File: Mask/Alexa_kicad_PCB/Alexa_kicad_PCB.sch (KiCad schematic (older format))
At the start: 28 parts

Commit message: changed op amp to tlv2372
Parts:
- removed U?: OPAMP, symbol pspice:OPAMP
- added U? (x2): TLV2372, symbol Amplifier_Operational:TLV2372
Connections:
- net labels added: EYES_SERVO, MOUTH_SERVO, NECK_SERVO
- wire segments 86 -> 100
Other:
- moved on the sheet: C?, M?, R?

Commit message: changed 3.5mm jack to 1503 09 part symbol
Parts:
- removed J?: Audio In, symbol Connector:AudioJack2_Ground
- removed J?: Audio Out, symbol Connector:AudioJack2_Ground
- added X? (x2): 1503_09, 1503_09, symbol Kicad_symbols:1503_09
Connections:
- wire segments 100 -> 104
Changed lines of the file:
@@
 	6200 4150 6200 4200
-$Comp
-L Connector:AudioJack2_Ground J?
-U 1 1 5F09035A
-P 1050 6350
-F 0 "J?" H 1082 6675 50  0000 C CNN
-F 1 "Audio In" H 1082 6584 50  0000 C CNN
-F 2 "" H 1050 6350 50  0001 C CNN
-F 3 "~" H 1050 6350 50  0001 C CNN
-	1    1050 6350
-	1    0    0    -1
-$EndComp
-$Comp
-L Connector:AudioJack2_Ground J?
-U 1 1 5F094637
-P 1050 7050
-F 0 "J?" H 1082 7375 50  0000 C CNN
-F 1 "Audio Out" H 1082 7284 50  0000 C CNN
-F 2 "" H 1050 7050 50  0001 C CNN
-F 3 "~" H 1050 7050 50  0001 C CNN
-	1    1050 7050
-	1    0    0    -1
-$EndComp
-Wire Wire Line
-	1250 6250 1400 6250
-Wire Wire Line
-	1400 6250 1400 6450
-Wire Wire Line
-	1400 6950 1250 6950
-Wire Wire Line
-	1250 6350 1450 6350
-Wire Wire Line
-	1450 6350 1450 6450
-Wire Wire Line
-	1450 7050 1250 7050
 $Comp
 L Device:R_Small R?
@@
 ADC_0
 $Comp
-L power:GND #PWR?
-U 1 1 5F1297DD
-P 1050 6500
-F 0 "#PWR?" H 1050 6250 50  0001 C CNN
-F 1 "GND" H 1150 6400 50  0000 C CNN
-F 2 "" H 1050 6500 50  0001 C CNN
-F 3 "" H 1050 6500 50  0001 C CNN
-	1    1050 6500
-	1    0    0    -1
-$EndComp
-$Comp
-L power:GND #PWR?
-U 1 1 5F12A17D
-P 1050 7250
-F 0 "#PWR?" H 1050 7000 50  0001 C CNN
-F 1 "GND" H 1150 7150 50  0000 C CNN
-F 2 "" H 1050 7250 50  0001 C CNN
-F 3 "" H 1050 7250 50  0001 C CNN
-	1    1050 7250
-	1    0    0    -1
-$EndComp
-Wire Wire Line
-	2200 6450 1450 6450
-Connection ~ 1450 6450
-Wire Wire Line
-	1450 6450 1450 7050
-Wire Wire Line
-	1450 6450 1400 6450
-Connection ~ 1400 6450
-Wire Wire Line
-	1400 6450 1400 6950
-$Comp
 L power:+5V #PWR?
 U 1 1 5F14761B
@@
 	1    0    0    -1
 $EndComp
+$Comp
+L Kicad_symbols:1503_09 X?
+U 1 1 5F24E4B9
+P 900 6300
+F 0 "X?" H 947 5886 50  0000 C CNN
+F 1 "1503_09" H 947 5977 50  0000 C CNN
+F 2 "1503_09" H 900 6300 50  0001 L BNN
+F 3 "unknown" H 900 6300 50  0001 L BNN
+F 4 "" H 900 6300 50  0001 L BNN "Field4"
+F 5 "" H 900 6300 50  0001 L BNN "Field5"
+F 6 "1243244" H 900 6300 50  0001 L BNN "Field6"
+F 7 "1" H 900 6300 50  0001 L BNN "Field7"
+	1    900  6300
+	-1   0    0    1
+$EndComp
+$Comp
+L Kicad_symbols:1503_09 X?
+U 1 1 5F2551EC
+P 900 7000
+F 0 "X?" H 947 6586 50  0000 C CNN
+F 1 "1503_09" H 947 6677 50  0000 C CNN
+F 2 "1503_09" H 900 7000 50  0001 L BNN
+F 3 "unknown" H 900 7000 50  0001 L BNN
+F 4 "" H 900 7000 50  0001 L BNN "Field4"
+F 5 "" H 900 7000 50  0001 L BNN "Field5"
+F 6 "1243244" H 900 7000 50  0001 L BNN "Field6"
+F 7 "1" H 900 7000 50  0001 L BNN "Field7"
+	1    900  7000
+	-1   0    0    1
+$EndComp
+$Comp
+L power:GND #PWR?
+U 1 1 5F256FB9
+P 1350 6100
+F 0 "#PWR?" H 1350 5850 50  0001 C CNN
+F 1 "GND" H 1350 6150 50  0000 C CNN
+F 2 "" H 1350 6100 50  0001 C CNN
+F 3 "" H 1350 6100 50  0001 C CNN
+	1    1350 6100
+	1    0    0    -1
+$EndComp
+$Comp
+L power:GND #PWR?
+U 1 1 5F2576E6
+P 1350 6800
+F 0 "#PWR?" H 1350 6550 50  0001 C CNN
+F 1 "GND" H 1350 6850 50  0000 C CNN
+F 2 "" H 1350 6800 50  0001 C CNN
+F 3 "" H 1350 6800 50  0001 C CNN
+	1    1350 6800
+	1    0    0    -1
+$EndComp
+Wire Wire Line
+	1100 6800 1350 6800
+Wire Wire Line
+	1100 6100 1350 6100
+Wire Wire Line
+	1100 6500 1200 6500
+Wire Wire Line
+	1200 6500 1200 6450
+Wire Wire Line
+	1200 6200 1100 6200
+Wire Wire Line
+	1100 6900 1200 6900
+Wire Wire Line
+	1200 6900 1200 7050
+Wire Wire Line
+	1200 7200 1100 7200
+Wire Wire Line
+	1200 6450 1500 6450
+Connection ~ 1200 6450
+Wire Wire Line
+	1200 6450 1200 6200
+Wire Wire Line
+	1200 7050 1500 7050
+Wire Wire Line
+	1500 7050 1500 6450
+Connection ~ 1200 7050
+Wire Wire Line
+	1200 7050 1200 7200
+Connection ~ 1500 6450
+Wire Wire Line
+	1500 6450 2200 6450
 $EndSCHEMATC

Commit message: all footprints matched to symbols
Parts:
- removed D?: 1N4001, symbol Device:D_Small
- added D1: BAR43FILM, Package_TO_SOT_SMD:SOT-23, symbol Diode:BAR43FILM
- C1, C4: renamed from C?; value 10p -> 18pf; footprint (none) -> Capacitor_SMD:C_0805_2012Metric
- C2, C3, C5, C6: renamed from C?; footprint (none) -> Capacitor_SMD:C_0805_2012Metric
- J1: renamed from J?; footprint (none) -> Connector_BarrelJack:BarrelJack_Wuerth_6941xx301002
- J2: renamed from J?; footprint (none) -> Connector_USB:USB_Micro-B_Molex-105017-0001
- M1, M2, M3: renamed from M?; footprint (none) -> Connector_PinHeader_2.54mm:PinHeader_1x03_P2.54mm_Horizontal
- R1, R10, R2, R3, R4, R5, R6, R7, R8, R9: renamed from R?; footprint (none) -> Resistor_SMD:R_0805_2012Metric
- U1: renamed from U?; footprint (none) -> Package_SO:SOIC-8_3.9x4.9mm_P1.27mm
- U2: renamed from U?; footprint (none) -> Package_TO_SOT_SMD:SOT-223-3_TabPin2
- X1, X2: renamed from X?; footprint 1503_09 -> kicad_footprints:1503_09
- Y1: renamed from Y?; footprint (none) -> Crystal:Crystal_SMD_Abracon_ABM3-2Pin_5.0x3.2mm
- gave numbers to parts that had none: 1

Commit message: routing completed
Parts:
- added D2: BAR43FILM, Package_TO_SOT_SMD:SOT-23, symbol Diode:BAR43FILM
- added J3: Conn_01x07_Male, Connector_PinHeader_2.54mm:PinHeader_1x07_P2.54mm_Horizontal, symbol Connector:Conn_01x07_Male
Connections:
- net +3V3: now also J3.7 (Pin_7)
- net +5V: now also D2.3 (K)
- net GND: now also J2.5 (GND), J2.6 (Shield), J3.6 (Pin_6)
- net 33_BO: now reaches U3.33 (PB12)
- net 33_BO: now also J3.5 (Pin_5)
- net 34_BO: now reaches U3.34 (PB13)
- net 34_BO: now also J3.4 (Pin_4)
- net 35_BO: now reaches U3.35 (PB14)
- net 35_BO: now also J3.3 (Pin_3)
- net 36_BO: now reaches U3.36 (PB15)
- net 36_BO: now also J3.2 (Pin_2)
- net 37_BO: now reaches U3.37 (PC6)
- net 37_BO: now also J3.1 (Pin_1)
- net 38_BO: now reaches U3.38 (PC7)
- net 39_BO: now reaches U3.39 (PC8)
- net 40_BO: now reaches U3.40 (PC9)
- net 41_BO: now reaches U3.41 (PA8)
- net 42_BO: now reaches U3.42 (PA9)
- net at J2.1 (VBUS): now also D2.1 (A)
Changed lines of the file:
@@
 	2950 6550 3000 6550
 Connection ~ 2950 6550
+$Comp
+L power:+5V #PWR0126
+U 1 1 5F2E15DC
+P 8650 850
+F 0 "#PWR0126" H 8650 700 50  0001 C CNN
+F 1 "+5V" H 8665 1023 50  0000 C CNN
+F 2 "" H 8650 850 50  0001 C CNN
+F 3 "" H 8650 850 50  0001 C CNN
+	1    8650 850
+	1    0    0    -1
+$EndComp
+Wire Wire Line
+	7900 1150 8050 1150
+$Comp
+L power:GND #PWR0127
+U 1 1 5F2E63BF
+P 7600 1850
+F 0 "#PWR0127" H 7600 1600 50  0001 C CNN
+F 1 "GND" H 7605 1677 50  0000 C CNN
+F 2 "" H 7600 1850 50  0001 C CNN
+F 3 "" H 7600 1850 50  0001 C CNN
+	1    7600 1850
+	1    0    0    -1
+$EndComp
+Wire Wire Line
+	7600 1750 7600 1800
+Wire Wire Line
+	7500 1750 7500 1800
+Wire Wire Line
+	7500 1800 7600 1800
+Connection ~ 7600 1800
+Wire Wire Line
+	7600 1800 7600 1850
+Text Label 5400 5150 0    50   ~ 0
+33_BO
+Text Label 5400 5250 0    50   ~ 0
+34_BO
+Text Label 5400 5350 0    50   ~ 0
+35_BO
+Text Label 5400 5450 0    50   ~ 0
+36_BO
+Text Label 3900 4550 2    50   ~ 0
+37_BO
+Text Label 3900 4650 2    50   ~ 0
+38_BO
+Text Label 3900 4750 2    50   ~ 0
+39_BO
+Text Label 3900 4850 2    50   ~ 0
+40_BO
+Text Label 5400 3050 0    50   ~ 0
+41_BO
+Text Label 5400 3150 0    50   ~ 0
+42_BO
+Wire Wire Line
+	5350 3050 5400 3050
+Wire Wire Line
+	5350 3150 5400 3150
+Wire Wire Line
+	3900 4550 3950 4550
+Wire Wire Line
+	3900 4650 3950 4650
+Wire Wire Line
+	3900 4750 3950 4750
+Wire Wire Line
+	3900 4850 3950 4850
+Wire Wire Line
+	5350 5150 5400 5150
+Wire Wire Line
+	5350 5250 5400 5250
+Wire Wire Line
+	5350 5350 5400 5350
+Wire Wire Line
+	5350 5450 5400 5450
+Text Label 10200 5850 2    50   ~ 0
+33_BO
+Text Label 10200 5950 2    50   ~ 0
+34_BO
+Text Label 10200 6050 2    50   ~ 0
+35_BO
+Text Label 10200 6150 2    50   ~ 0
+36_BO
+Text Label 10200 6250 2    50   ~ 0
+37_BO
+$Comp
+L Connector:Conn_01x07_Male J3
+U 1 1 5F2F9C7F
+P 10450 5950
+F 0 "J3" H 10422 5882 50  0000 R CNN
+F 1 "Conn_01x07_Male" H 10422 5973 50  0000 R CNN
+F 2 "Connector_PinHeader_2.54mm:PinHeader_1x07_P2.54mm_Horizontal" H 10450 5950 50  0001 C CNN
+F 3 "~" H 10450 5950 50  0001 C CNN
+	1    10450 5950
+	-1   0    0    1
+$EndComp
+$Comp
+L power:GND #PWR0128
+U 1 1 5F30498A
+P 9800 5750
+F 0 "#PWR0128" H 9800 5500 50  0001 C CNN
+F 1 "GND" H 9805 5577 50  0000 C CNN
+F 2 "" H 9800 5750 50  0001 C CNN
+F 3 "" H 9800 5750 50  0001 C CNN
+	1    9800 5750
+	1    0    0    -1
+$EndComp
+$Comp
+L power:+3V3 #PWR0129
+U 1 1 5F304E92
+P 9800 5600
+F 0 "#PWR0129" H 9800 5450 50  0001 C CNN
+F 1 "+3V3" H 9815 5773 50  0000 C CNN
+F 2 "" H 9800 5600 50  0001 C CNN
+F 3 "" H 9800 5600 50  0001 C CNN
+	1    9800 5600
+	1    0    0    -1
+$EndComp
+Wire Wire Line
+	9800 5600 9800 5650
+Wire Wire Line
+	9800 5650 10250 5650
+Wire Wire Line
+	9800 5750 10250 5750
+Wire Wire Line
+	10200 6250 10250 6250
+Wire Wire Line
+	10200 6150 10250 6150
+Wire Wire Line
+	10200 6050 10250 6050
+Wire Wire Line
+	10200 5950 10250 5950
+Wire Wire Line
+	10200 5850 10250 5850
 Wire Wire Line
 	3300 6550 3400 6550
 Connection ~ 3400 6550
+$Comp
+L Diode:BAR43FILM D2
+U 1 1 5F3107B3
+P 8300 950
+F 0 "D2" H 8300 734 50  0000 C CNN
+F 1 "BAR43FILM" H 8300 825 50  0000 C CNN
+F 2 "Package_TO_SOT_SMD:SOT-23" H 8300 775 50  0001 C CNN
+F 3 "www.st.com/resource/en/datasheet/bar43.pdf" H 8300 950 50  0001 C CNN
+	1    8300 950
+	-1   0    0    1
+$EndComp
+Wire Wire Line
+	8050 950  8150 950
+Wire Wire Line
+	8050 950  8050 1150
+Wire Wire Line
+	8450 950  8650 950
+Wire Wire Line
+	8650 950  8650 850
 $EndSCHEMATC

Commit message: cleaned up dfu pullups on schematic - added buttons
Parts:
- removed R3, R5, R6, R7, R8: 100k, Resistor_SMD:R_0805_2012Metric, symbol Device:R_Small
- added R? (x4): 100K, symbol Device:R
- added R? (x2): 4K7, symbol Device:R
- added R? (x2): 10K, symbol Device:R
- added SW? (x3): SW_Push, symbol Switch:SW_Push
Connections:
- net +3V3: now also R?.2, R?.2, R?.2, R?.2, SW?.2
- net GND: now also R?.2, R?.2, R?.2, R?.2, SW?.1, SW?.1
- net PB2-(DFU): now reaches U3.28 (PB2)
- net PB2-(DFU): now also R?.1
- net PB11-(DFU): now reaches U3.30 (PB11)
- net PB11-(DFU): now also R?.1
- net PA10-(DFU): now reaches U3.43 (PA10)
- net PA10-(DFU): now also R?.1
- net PC11-(DFU): now reaches U3.52 (PC11)
- net PC11-(DFU): now also R?.1
- net PB5-(DFU): now reaches U3.57 (PB5)
- net PB5-(DFU): now also R?.1
- net BOOT0-(DFU): now reaches U3.60 (BOOT0)
- net BOOT0-(DFU): now also R?.1, SW?.1
- new net NRST: R?.1, SW?.2
- new net USR_SW: R?.1, SW?.2
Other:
- moved on the sheet: J3, M1, M2, M3

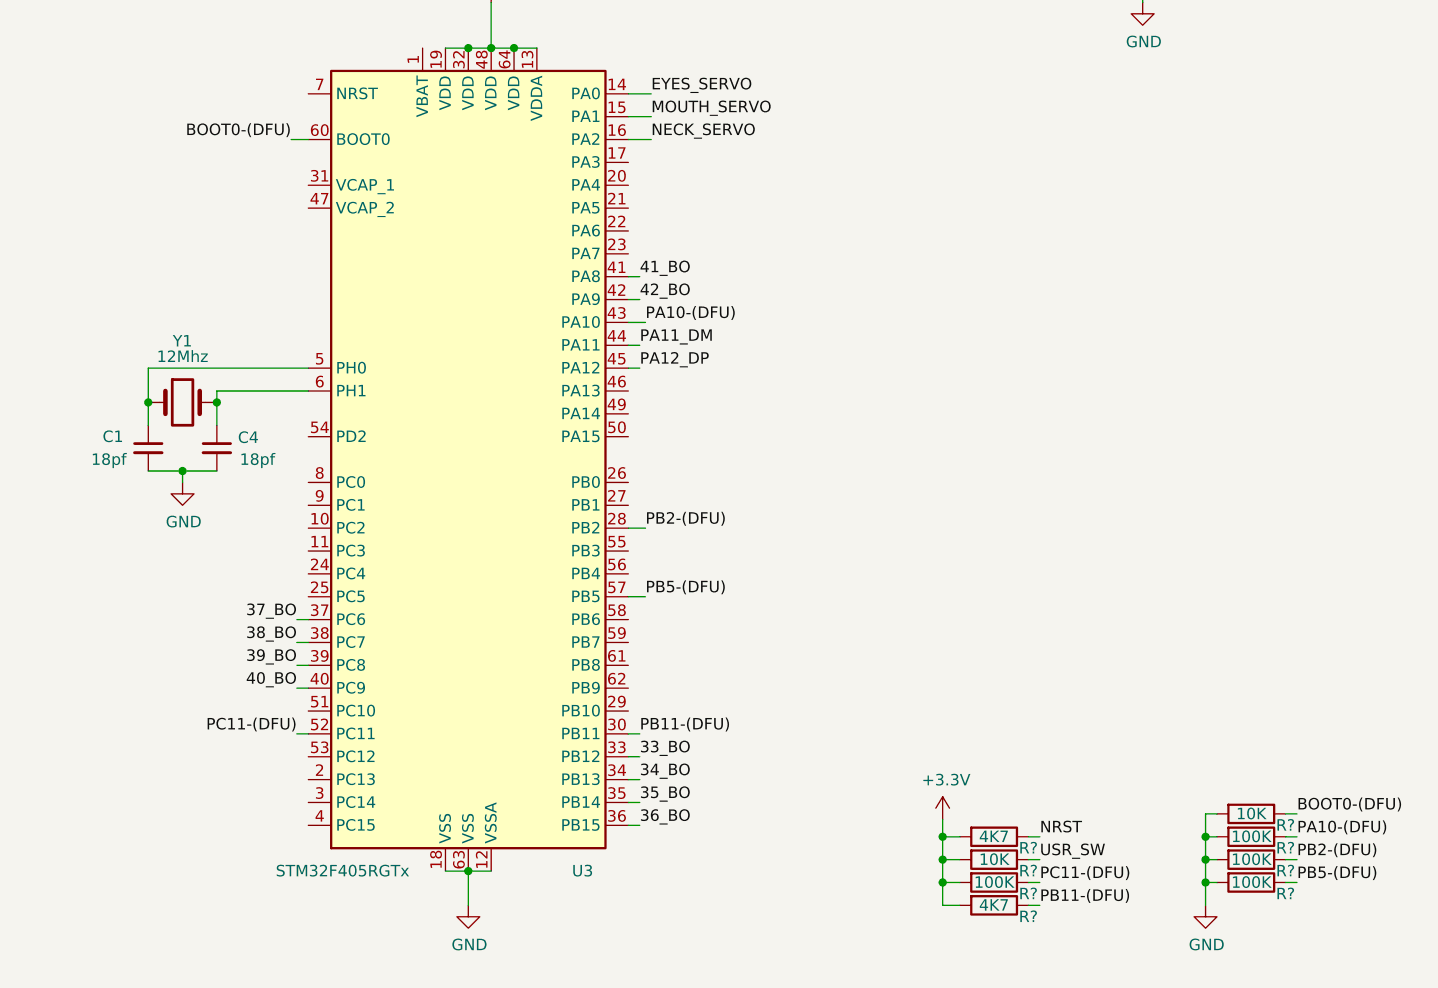
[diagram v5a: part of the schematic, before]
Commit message: added vcap caps
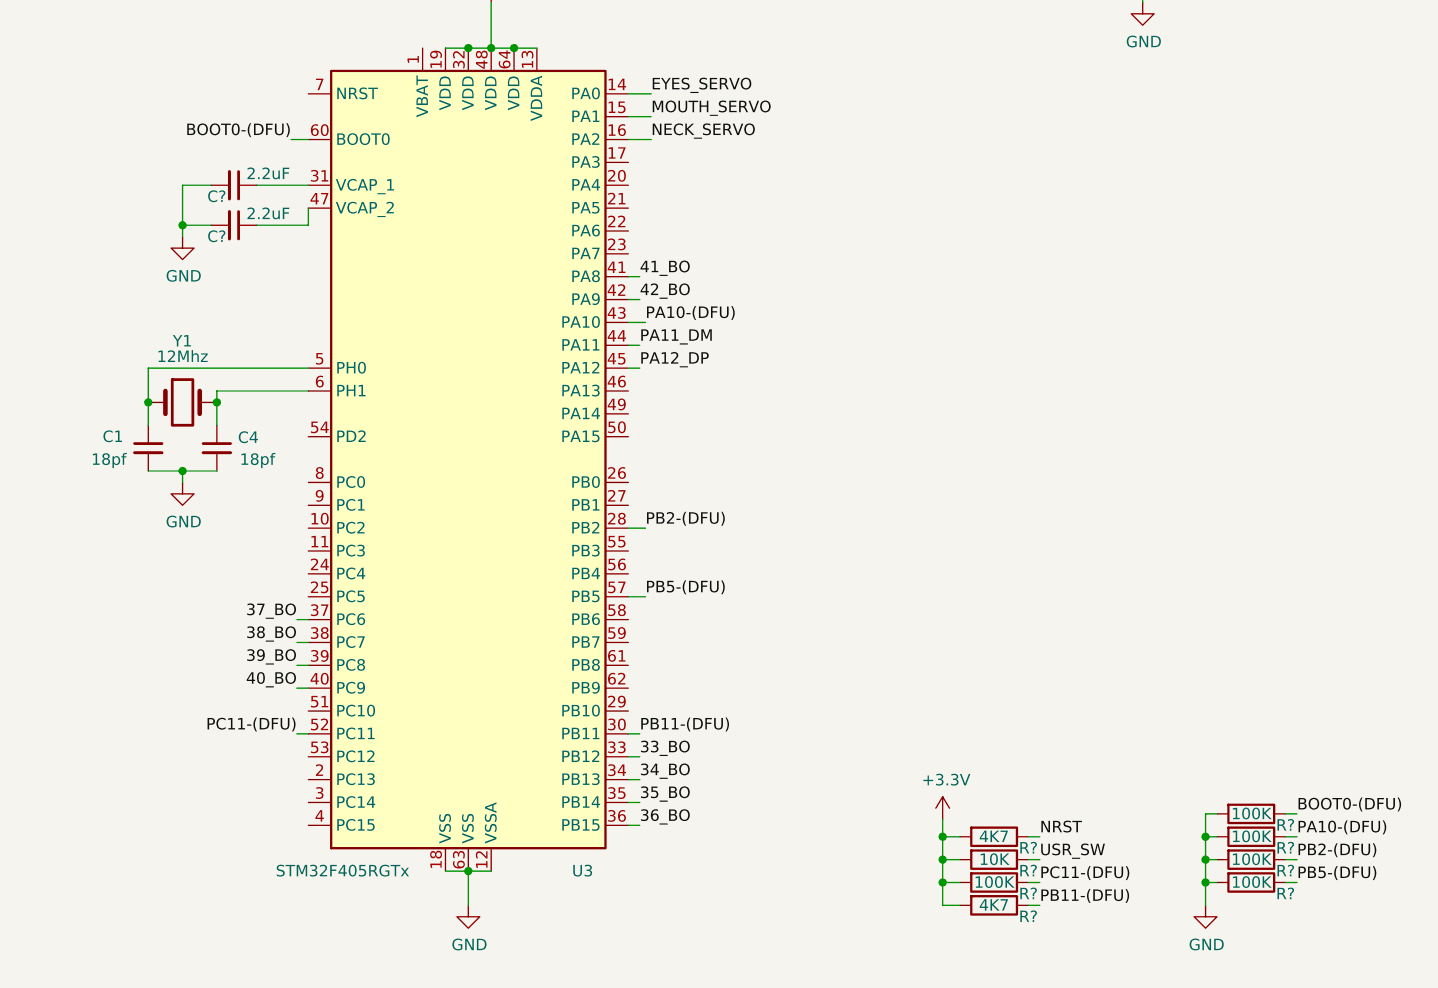
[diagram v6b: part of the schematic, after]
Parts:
- added C? (x2): 2.2uF, symbol Device:C_Small
- R?: value 10K -> 100K
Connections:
- net GND: now also C?.2, C?.2
- net at U3.31 (VCAP_1): now also C?.1
- net at U3.47 (VCAP_2): now also C?.1
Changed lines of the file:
@@
 P 8075 5400
 F 0 "R?" V 8125 5550 50  0000 C CNN
-F 1 "10K" V 8075 5400 50  0000 C CNN
+F 1 "100K" V 8075 5400 50  0000 C CNN
 F 2 "" V 8005 5400 50  0001 C CNN
 F 3 "~" H 8075 5400 50  0001 C CNN
@@
 Wire Wire Line
 	7100 5800 7150 5800
+$Comp
+L Device:C_Small C?
+U 1 1 5F7C528B
+P 3625 2650
+F 0 "C?" V 3675 2575 50  0000 C CNN
+F 1 "2.2uF" V 3575 2800 50  0000 C CNN
+F 2 "" H 3625 2650 50  0001 C CNN
+F 3 "~" H 3625 2650 50  0001 C CNN
+	1    3625 2650
+	0    1    1    0
+$EndComp
+$Comp
+L Device:C_Small C?
+U 1 1 5F7C7310
+P 3625 2825
+F 0 "C?" V 3675 2750 50  0000 C CNN
+F 1 "2.2uF" V 3575 2975 50  0000 C CNN
+F 2 "" H 3625 2825 50  0001 C CNN
+F 3 "~" H 3625 2825 50  0001 C CNN
+	1    3625 2825
+	0    1    1    0
+$EndComp
+Wire Wire Line
+	3950 2650 3725 2650
+Wire Wire Line
+	3950 2750 3950 2825
+Wire Wire Line
+	3950 2825 3725 2825
+$Comp
+L power:GND #PWR?
+U 1 1 5F7D6C7A
+P 3400 2875
+F 0 "#PWR?" H 3400 2625 50  0001 C CNN
+F 1 "GND" H 3405 2702 50  0000 C CNN
+F 2 "" H 3400 2875 50  0001 C CNN
+F 3 "" H 3400 2875 50  0001 C CNN
+	1    3400 2875
+	1    0    0    -1
+$EndComp
+Wire Wire Line
+	3525 2650 3400 2650
+Wire Wire Line
+	3400 2650 3400 2825
+Wire Wire Line
+	3525 2825 3400 2825
+Connection ~ 3400 2825
+Wire Wire Line
+	3400 2825 3400 2875
 $EndSCHEMATC
